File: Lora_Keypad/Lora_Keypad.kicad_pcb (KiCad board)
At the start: 2 copper layers, 66 x 91.4 mm, 2 parts, among them U1 Heltec_Wifi_LoRa_V1

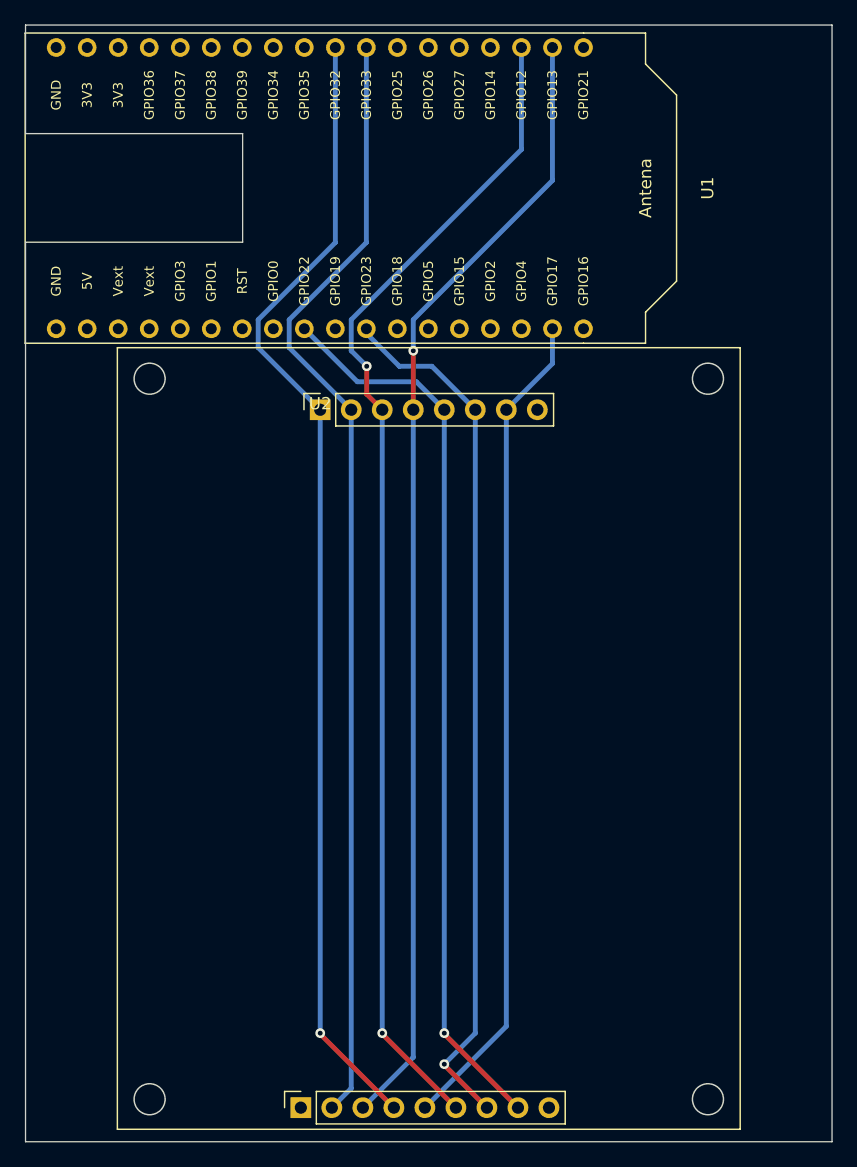
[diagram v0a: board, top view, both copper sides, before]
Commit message: added debug header
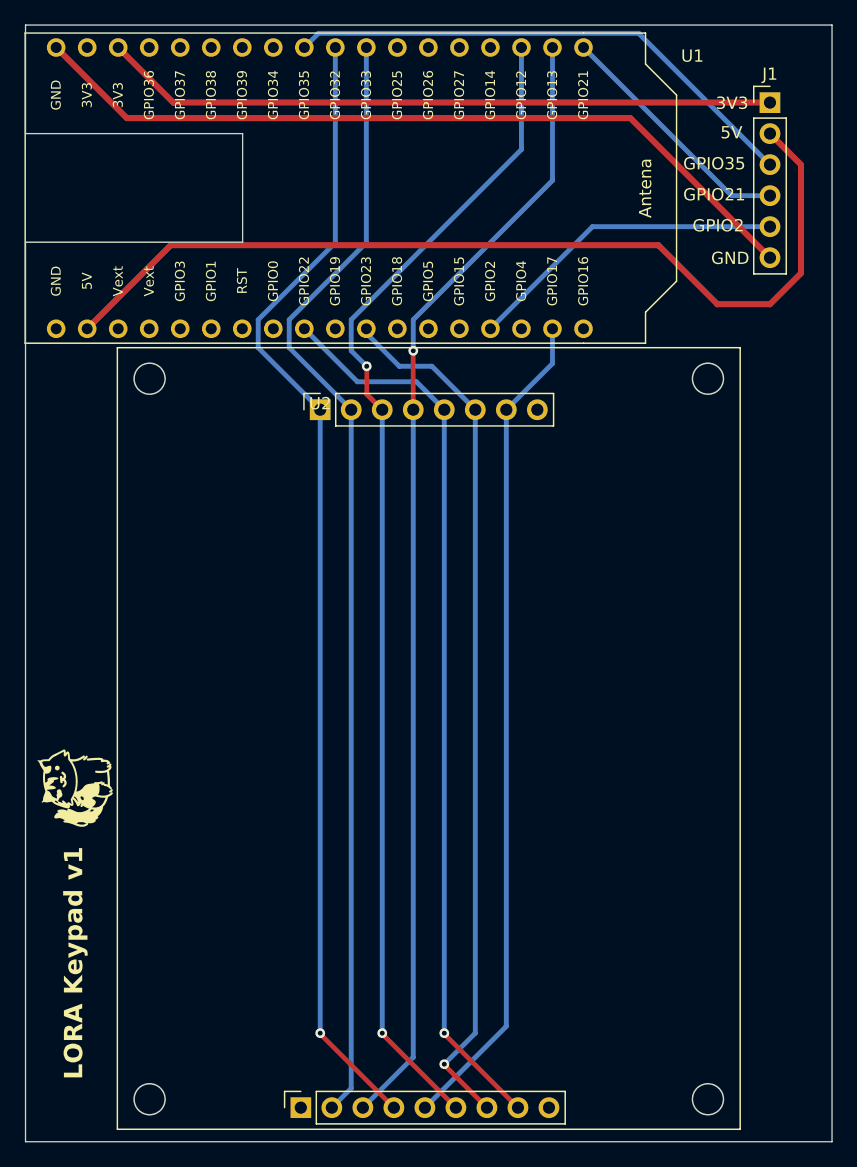
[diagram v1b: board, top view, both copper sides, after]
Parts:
- added G***: LOGO, Scotts:chewi_10, F.Cu at (116.3, 110.9)
- added J1: Debug, Connector_PinHeader_2.54mm:PinHeader_1x06_P2.54mm_Vertical, F.Cu at (174.0, 54.6)
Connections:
- U1 pad 15: unconnected-(U1-TOUCH2/HSPI_WP/ADC2_2/GPIO2-Pad15) -> Net-(J1-Pin_5)
- U1 pad 19: unconnected-(U1-V_SPI_HD/SDA/GPIO21-Pad19) -> Net-(J1-Pin_4)
- U1 pad 2: unconnected-(U1-5V-Pad2) -> +5V
- U1 pad 28: unconnected-(U1-ADC1_7/GPIO35-Pad28) -> Net-(J1-Pin_3)
- U1 pad 34: unconnected-(U1-3V3-Pad34) -> +3.3V
- U1 pad 36: unconnected-(U1-GND-Pad36) -> GND
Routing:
- net +5V: track 0.00 -> 76.8 mm
- net GND: track 0.00 -> 65.6 mm
- net +3.3V: track 0.00 -> 55.2 mm
- net Net-(J1-Pin_3): track 0.00 -> 43.1 mm
- net Net-(J1-Pin_5): track 0.00 -> 26.4 mm
- net Net-(J1-Pin_4): track 0.00 -> 20.3 mm
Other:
- board text added: "${TITLE} ${REVISION}"
- board text added: "3V3"
- board text added: "5V"
- board text added: "GND"
- board text added: "GPIO2"
- board text added: "GPIO21"
- board text added: "GPIO35"

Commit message: added mounting wholes
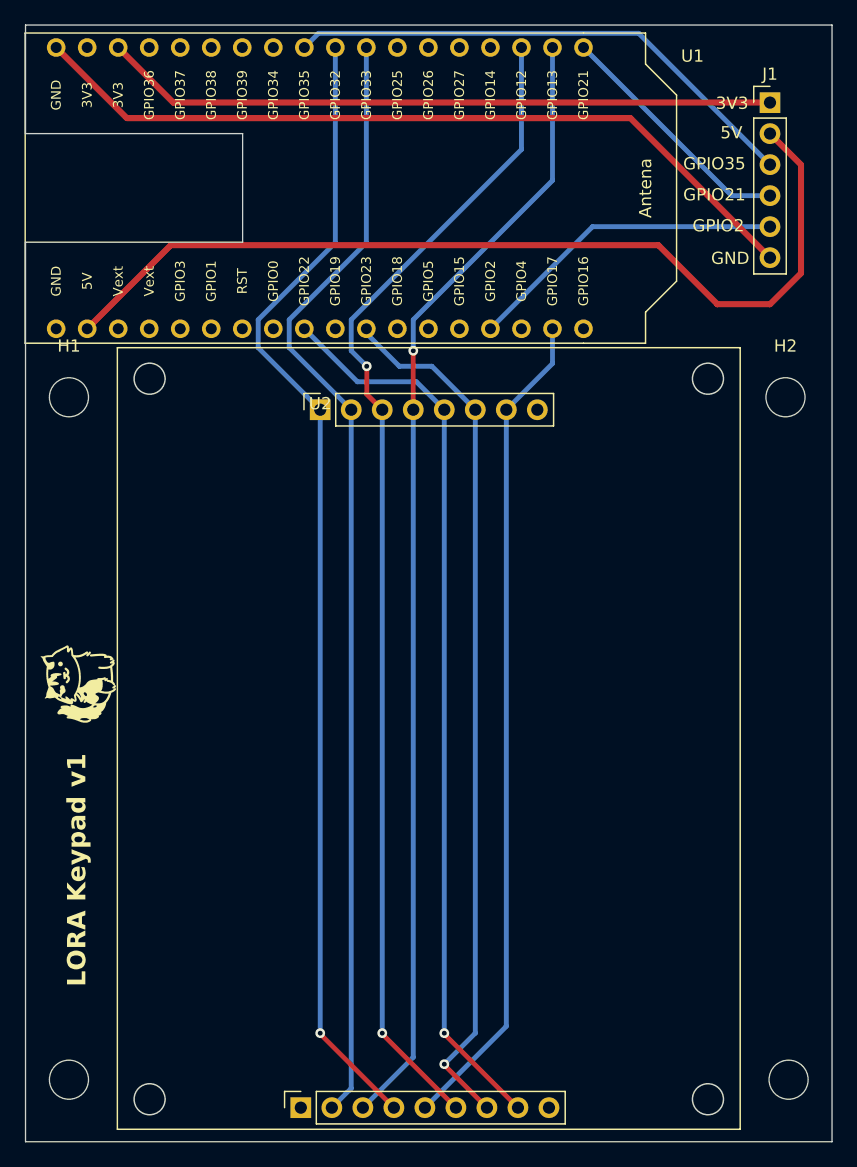
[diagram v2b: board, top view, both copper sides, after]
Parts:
- added H1: MountingHole, MountingHole:MountingHole_3.2mm_M3, F.Cu at (116.6, 78.7)
- added H2: MountingHole, MountingHole:MountingHole_3.2mm_M3, F.Cu at (175.3, 78.7)
- added H3: MountingHole, MountingHole:MountingHole_3.2mm_M3, F.Cu at (116.6, 134.6)
- added H4: MountingHole, MountingHole:MountingHole_3.2mm_M3, F.Cu at (175.5, 134.6)
- moved G*** 8.53 mm to (116.6, 102.4)
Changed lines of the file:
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@@
     (property "ki_description" "Generic connector, single row, 01x06, script generated")
     (property "ki_keywords" "connector")
-    (attr through_hole)
+    (attr through_hole exclude_from_pos_files)
     (fp_text reference "J1" (at 0 -2.33) (layer "F.SilkS")
         (effects (font (size 1 1) (thickness 0.15)))
@@
   )
   (footprint "Scotts:chewi_10" (layer "F.Cu")
-    (at 116.32498 110.883109 90)
+    (at 116.586 102.362 90)
     (attr board_only exclude_from_pos_files exclude_from_bom)
     (fp_text reference "G***" (at -0.4572 -2.3622 90) (layer "Dwgs.User")
@@
       (stroke (width 0) (type solid)) (fill solid) (layer "F.SilkS"))
   )
+  (footprint "MountingHole:MountingHole_3.2mm_M3" (layer "F.Cu")
+    (at 116.586 134.62)
+    (descr "Mounting Hole 3.2mm, no annular, M3")
+    (tags "mounting hole 3.2mm no annular m3")
+    (property "Sheetfile" "Lora_Keypad.kicad_sch")
+    (property "Sheetname" "")
+    (property "ki_description" "Mounting Hole without connection")
+    (property "ki_keywords" "mounting hole")
+    (attr exclude_from_pos_files exclude_from_bom)
+    (fp_text reference "H3" (at 0 -4.2) (layer "F.Fab")
+        (effects (font (size 1 1) (thickness 0.15)))
+    )
+    (fp_text value "MountingHole" (at 0 4.2) (layer "F.Fab")
+        (effects (font (size 1 1) (thickness 0.15)))
+    )
+    (fp_text user "${REFERENCE}" (at 0 0) (layer "F.Fab")
+        (effects (font (size 1 1) (thickness 0.15)))
+    )
+    (fp_circle (center 0 0) (end 3.2 0)
+      (stroke (width 0.15) (type solid)) (fill none) (layer "Cmts.User"))
+    (fp_circle (center 0 0) (end 3.45 0)
+      (stroke (width 0.05) (type solid)) (fill none) (layer "F.CrtYd"))
+    (pad "" np_thru_hole circle (at 0 0) (size 3.2 3.2) (drill 3.2) (layers "*.Cu" "*.Mask"))
+  )
+  (footprint "MountingHole:MountingHole_3.2mm_M3" (layer "F.Cu")
+    (at 116.586 78.74)
+    (descr "Mounting Hole 3.2mm, no annular, M3")
+    (tags "mounting hole 3.2mm no annular m3")
+    (property "Sheetfile" "Lora_Keypad.kicad_sch")
+    (property "Sheetname" "")
+    (property "ki_description" "Mounting Hole without connection")
+    (property "ki_keywords" "mounting hole")
+    (attr exclude_from_pos_files exclude_from_bom)
+    (fp_text reference "H1" (at 0 -4.2) (layer "F.SilkS")
+        (effects (font (size 1 1) (thickness 0.15)))
+    )
+    (fp_text value "MountingHole" (at 0 4.2) (layer "F.Fab")
+        (effects (font (size 1 1) (thickness 0.15)))
+    )
+    (fp_text user "${REFERENCE}" (at 0 0) (layer "F.Fab")
+        (effects (font (size 1 1) (thickness 0.15)))
+    )
+    (fp_circle (center 0 0) (end 3.2 0)
+      (stroke (width 0.15) (type solid)) (fill none) (layer "Cmts.User"))
+    (fp_circle (center 0 0) (end 3.45 0)
+      (stroke (width 0.05) (type solid)) (fill none) (layer "F.CrtYd"))
+    (pad "" np_thru_hole circle (at 0 0) (size 3.2 3.2) (drill 3.2) (layers "*.Cu" "*.Mask"))
+  )
+  (footprint "MountingHole:MountingHole_3.2mm_M3" (layer "F.Cu")
+    (at 175.26 78.74)
+    (descr "Mounting Hole 3.2mm, no annular, M3")
+    (tags "mounting hole 3.2mm no annular m3")
+    (property "Sheetfile" "Lora_Keypad.kicad_sch")
+    (property "Sheetname" "")
+    (property "ki_description" "Mounting Hole without connection")
+    (property "ki_keywords" "mounting hole")
+    (attr exclude_from_pos_files exclude_from_bom)
+    (fp_text reference "H2" (at 0 -4.2) (layer "F.SilkS")
+        (effects (font (size 1 1) (thickness 0.15)))
+    )
+    (fp_text value "MountingHole" (at 0 4.2) (layer "F.Fab")
+        (effects (font (size 1 1) (thickness 0.15)))
+    )
+    (fp_text user "${REFERENCE}" (at 0 0) (layer "F.Fab")
+        (effects (font (size 1 1) (thickness 0.15)))
+    )
+    (fp_circle (center 0 0) (end 3.2 0)
+      (stroke (width 0.15) (type solid)) (fill none) (layer "Cmts.User"))
+    (fp_circle (center 0 0) (end 3.45 0)
+      (stroke (width 0.05) (type solid)) (fill none) (layer "F.CrtYd"))
+    (pad "" np_thru_hole circle (at 0 0) (size 3.2 3.2) (drill 3.2) (layers "*.Cu" "*.Mask"))
+  )
+  (footprint "MountingHole:MountingHole_3.2mm_M3" (layer "F.Cu")
+    (at 175.514 134.62)
+    (descr "Mounting Hole 3.2mm, no annular, M3")
+    (tags "mounting hole 3.2mm no annular m3")
+    (property "Sheetfile" "Lora_Keypad.kicad_sch")
+    (property "Sheetname" "")
+    (property "ki_description" "Mounting Hole without connection")
+    (property "ki_keywords" "mounting hole")
+    (attr exclude_from_pos_files exclude_from_bom)
+    (fp_text reference "H4" (at 0 -4.2) (layer "F.Fab")
+        (effects (font (size 1 1) (thickness 0.15)))
+    )
+    (fp_text value "MountingHole" (at 0 4.2) (layer "F.Fab")
+        (effects (font (size 1 1) (thickness 0.15)))
+    )
+    (fp_text user "${REFERENCE}" (at 0 0) (layer "F.Fab")
+        (effects (font (size 1 1) (thickness 0.15)))
+    )
+    (fp_circle (center 0 0) (end 3.2 0)
+      (stroke (width 0.15) (type solid)) (fill none) (layer "Cmts.User"))
+    (fp_circle (center 0 0) (end 3.45 0)
+      (stroke (width 0.05) (type solid)) (fill none) (layer "F.CrtYd"))
+    (pad "" np_thru_hole circle (at 0 0) (size 3.2 3.2) (drill 3.2) (layers "*.Cu" "*.Mask"))
+  )
   (gr_line (start 130.81 57.15) (end 113.03 57.15)
     (stroke (width 0.1) (type default)) (layer "Edge.Cuts"))
@@
     (effects (font (size 1 1) (thickness 0.15)) (justify left bottom))
   )
-  (gr_text "${TITLE} ${REVISION}" (at 117.856 134.62 90) (layer "F.SilkS")
+  (gr_text "${TITLE} ${REVISION}" (at 118.11 127 90) (layer "F.SilkS")
     (effects (font (size 1.5 1.5) (thickness 0.3) bold) (justify left bottom))
   )

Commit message: add plug in 3 to 4 adapter
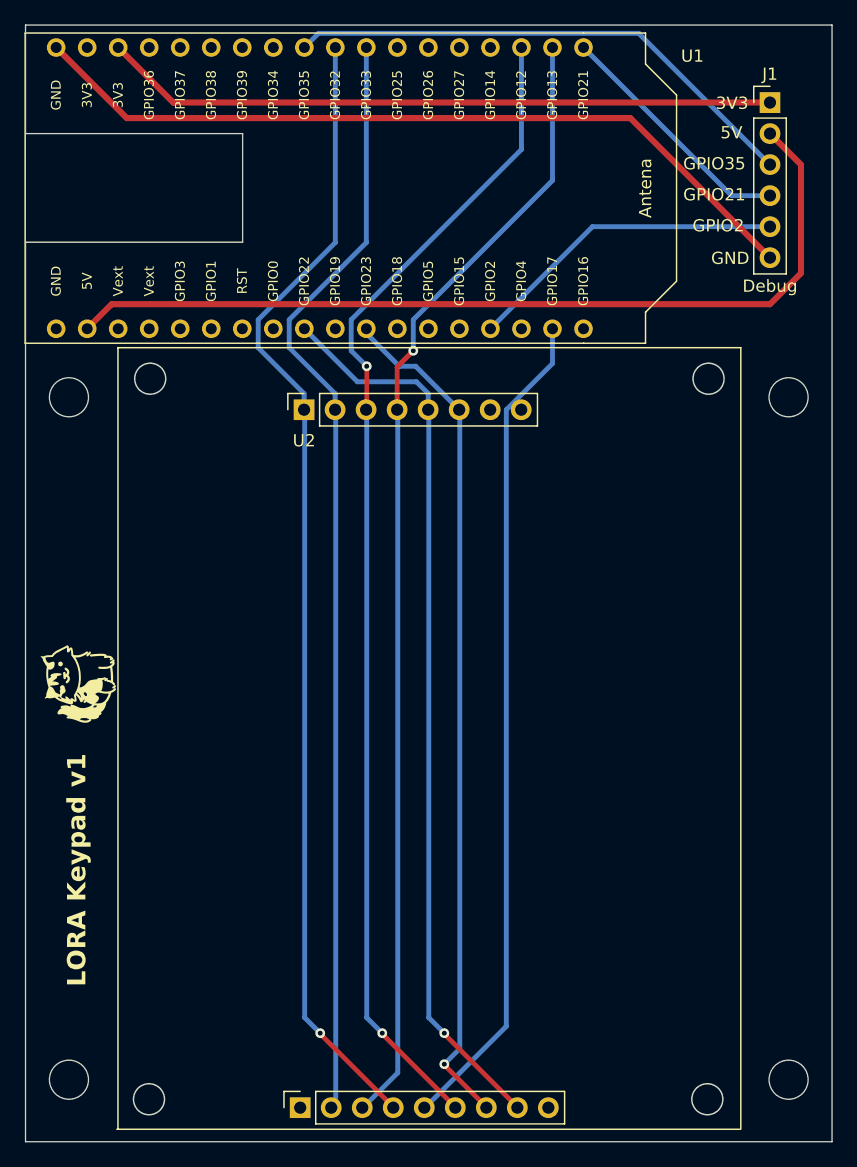
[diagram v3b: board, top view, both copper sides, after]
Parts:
- moved U2 1.32 mm to (135.8, 79.8)
- moved H2 0.25 mm to (175.5, 78.7)
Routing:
- net +5V: track 76.8 -> 72.8 mm
- net R3: track 71.5 -> 69.7 mm
- net C2: track 92.2 -> 91.1 mm
